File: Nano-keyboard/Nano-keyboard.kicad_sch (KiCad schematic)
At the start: 45 parts, among them J1 125SH-B-04-TS, J2 125SH-B-02-TS, U1 AMS1117, U2 ESP32-WROOM-32, U3 J5019, U4 QBC847BL, U5 EN12-HN22AF25, U6 EN12-HN22AF25, U7 QBC847BL, U8 QBC847BL

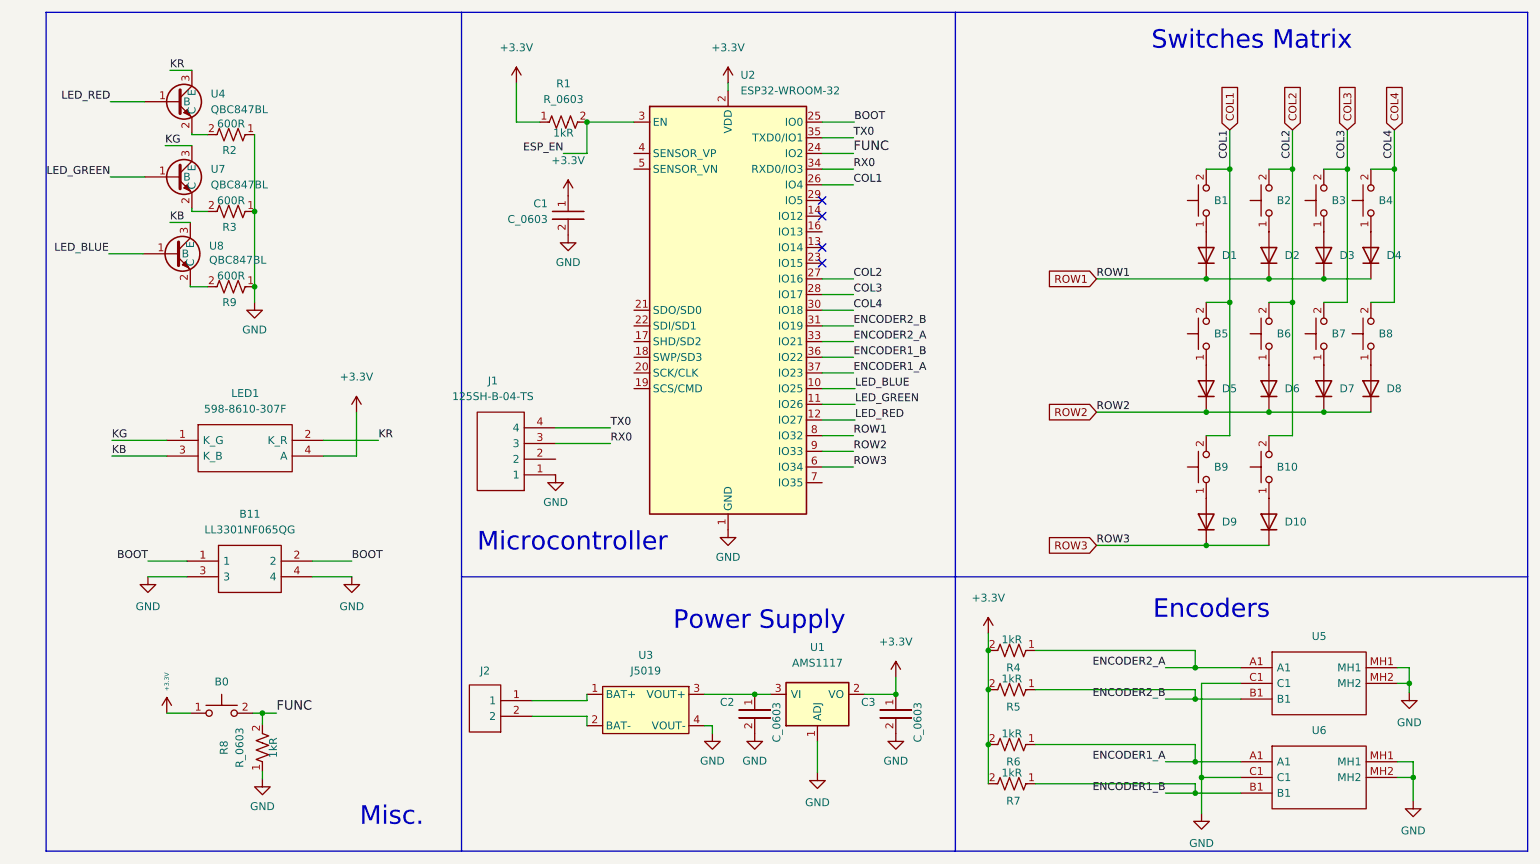
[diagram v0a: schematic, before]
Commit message: Routing of version 1.2 almest finished
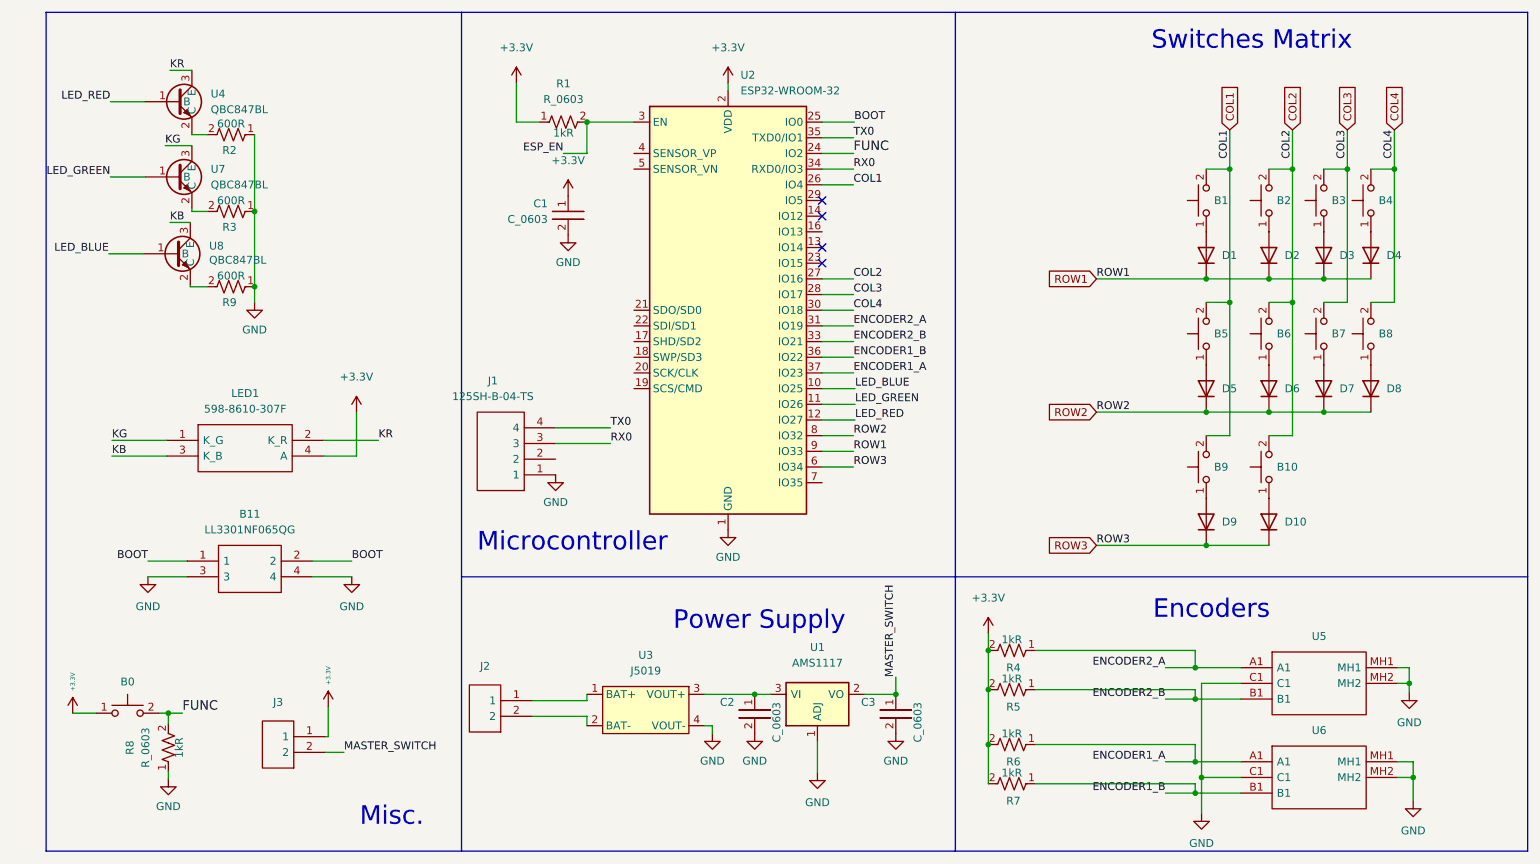
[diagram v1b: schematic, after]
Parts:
- removed J2: 125SH-B-02-TS, lib:125SHB02TS, symbol custom-keyboard:125SH-B-02-TS
- added J2, J3: 25SH-B-02-TS, lib:25SHB02TS, symbol custom-keyboard:25SH-B-02-TS
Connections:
- net +3V3: now also J3.1; no longer C3.1, U1.2 (VO)
- net ENCODER2_A: now also U2.31 (IO19); no longer U2.33 (IO21)
- net ENCODER2_B: now also U2.33 (IO21); no longer U2.31 (IO19)
- net ROW1: now also U2.9 (IO33); no longer U2.8 (IO32)
- net ROW2: now also U2.8 (IO32); no longer U2.9 (IO33)
- net at U3.1 (BAT+): now also J2.1
- net at U3.2 (BAT-): now also J2.2
- new net MASTER_SWITCH: C3.1, J3.2, U1.2 (VO)
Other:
- moved on the sheet: B0, R8

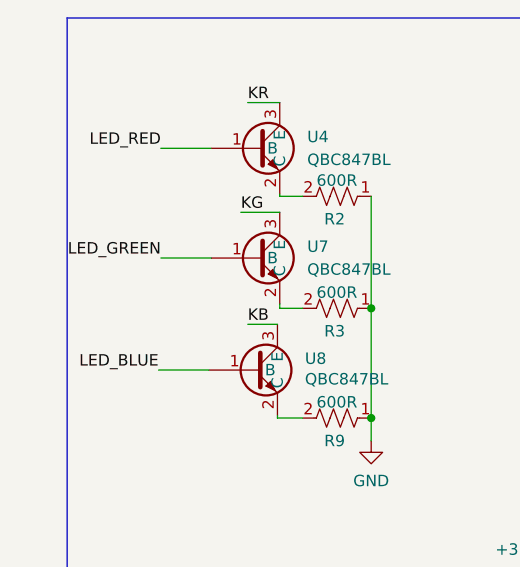
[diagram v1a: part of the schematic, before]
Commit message: Addded more spacing between keys and encoder
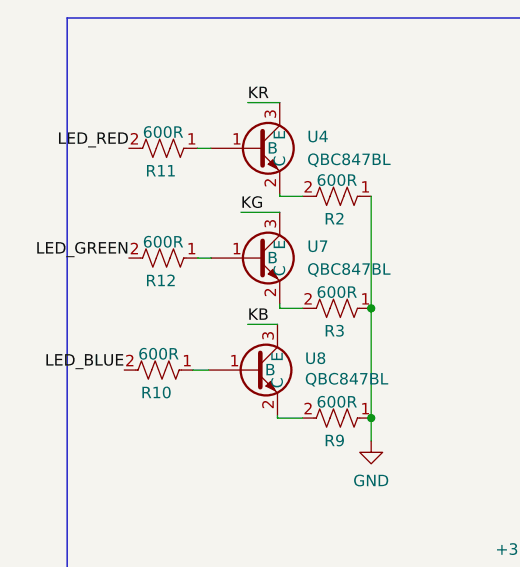
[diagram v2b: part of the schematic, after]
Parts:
- added R10, R11, R12: R_0603, lib:R_0603_1608Metric, symbol custom-keyboard:R_0603
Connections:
- net LED_BLUE: now also R10.2; no longer U8.1 (B)
- net LED_GREEN: now also R12.2; no longer U7.1 (B)
- net LED_RED: now also R11.2; no longer U4.1 (B)
- new net: R11.1, U4.1 (B)
- new net: R10.1, U8.1 (B)
- new net: R12.1, U7.1 (B)
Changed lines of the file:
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@@
     (stroke (width 0) (type default) (color 0 0 0 0))
   )
-  (wire (pts (xy 46.228 67.056) (xy 40.64 67.056))
+  (wire (pts (xy 46.228 67.056) (xy 44.45 67.056))
     (stroke (width 0) (type default) (color 0 0 0 0))
   )
@@
     (stroke (width 0) (type default) (color 0 0 0 0))
   )
-  (wire (pts (xy 46.482 54.61) (xy 40.894 54.61))
+  (wire (pts (xy 46.482 54.61) (xy 44.958 54.61))
     (stroke (width 0) (type default) (color 0 0 0 0))
   )
@@
     (stroke (width 0) (type default) (color 0 0 0 0))
   )
-  (wire (pts (xy 46.482 42.418) (xy 40.894 42.418))
+  (wire (pts (xy 46.482 42.418) (xy 44.958 42.418))
     (stroke (width 0) (type default) (color 0 0 0 0))
   )
@@
     (effects (font (size 1.27 1.27)) (justify left bottom))
   )
+  (label "LED_RED" (at 37.338 42.418 180)
+    (effects (font (size 1.27 1.27)) (justify right bottom))
+  )
   (label "MASTER_SWITCH" (at 78.74 147.828 0)
     (effects (font (size 1.27 1.27)) (justify left bottom))
@@
     (effects (font (size 1.27 1.27)) (justify left bottom))
   )
-  (label "LED_BLUE" (at 40.64 67.056 180)
-    (effects (font (size 1.27 1.27)) (justify right bottom))
-  )
   (label "ESP_EN" (at 114.3 50.8 180)
     (effects (font (size 1.27 1.27)) (justify right bottom))
@@
     (effects (font (size 1.27 1.27)) (justify left bottom))
   )
+  (label "LED_GREEN" (at 37.338 54.61 180)
+    (effects (font (size 1.27 1.27)) (justify right bottom))
+  )
   (label "FUNC" (at 52.578 141.478 0)
     (effects (font (size 1.524 1.524)) (justify left bottom))
@@
     (effects (font (size 1.27 1.27)) (justify left bottom))
   )
+  (label "LED_BLUE" (at 36.83 67.056 180)
+    (effects (font (size 1.27 1.27)) (justify right bottom))
+  )
   (label "KB" (at 41.148 99.822 0)
     (effects (font (size 1.27 1.27)) (justify left bottom))
@@
     (effects (font (size 1.27 1.27)) (justify right bottom))
   )
-  (label "LED_RED" (at 40.894 42.418 180)
-    (effects (font (size 1.27 1.27)) (justify right bottom))
-  )
   (label "BOOT" (at 46.99 116.84 180)
     (effects (font (size 1.27 1.27)) (justify right bottom))
@@
   (label "ROW3" (at 200.66 114.3 0)
     (effects (font (size 1.27 1.27)) (justify left bottom))
-  )
-  (label "LED_GREEN" (at 40.894 54.61 180)
-    (effects (font (size 1.27 1.27)) (justify right bottom))
   )
   (label "RX0" (at 121.92 97.79 0)
@@
     )
     (pin "1")
+  )
+  (symbol (lib_id "custom-keyboard:R_0603") (at 41.402 42.418 270) (unit 1)
+    (in_bom yes) (on_board yes)
+    (property "Reference" "R11" (id 0) (at 40.894 44.958 90))
+    (property "Value" "R_0603" (id 1) (at 41.148 46.101 90)
+      (effects (font (size 1.27 1.27)) hide)
+    )
+    (property "Footprint" "lib:R_0603_1608Metric" (id 2) (at 41.402 42.418 0)
+      (effects (font (size 1.27 1.27)) hide)
+    )
+    (property "Datasheet" "" (id 3) (at 41.402 42.418 0)
+      (effects (font (size 1.27 1.27)) hide)
+    )
+    (property "Resistance" "600R" (id 4) (at 41.148 41.402 90)
+      (effects (font (size 1.27 1.27)) (justify bottom))
+    )
+    (pin "1")
+    (pin "2")
   )
   (symbol (lib_id "custom-keyboard:Cherry_Switch_1U_PCB") (at 237.49 58.42 90) (unit 1)
@@
     (pin "2")
   )
+  (symbol (lib_id "custom-keyboard:R_0603") (at 40.894 67.056 270) (unit 1)
+    (in_bom yes) (on_board yes)
+    (property "Reference" "R10" (id 0) (at 40.386 69.596 90))
+    (property "Value" "R_0603" (id 1) (at 40.64 70.739 90)
+      (effects (font (size 1.27 1.27)) hide)
+    )
+    (property "Footprint" "lib:R_0603_1608Metric" (id 2) (at 40.894 67.056 0)
+      (effects (font (size 1.27 1.27)) hide)
+    )
+    (property "Datasheet" "" (id 3) (at 40.894 67.056 0)
+      (effects (font (size 1.27 1.27)) hide)
+    )
+    (property "Resistance" "600R" (id 4) (at 40.64 66.04 90)
+      (effects (font (size 1.27 1.27)) (justify bottom))
+    )
+    (pin "1")
+    (pin "2")
+  )
   (symbol (lib_id "custom-keyboard:EN12-HN22AF25") (at 224.028 134.112 0) (unit 1)
     (in_bom yes) (on_board yes) (fields_autoplaced)
@@
     (pin "2")
   )
+  (symbol (lib_id "custom-keyboard:R_0603") (at 41.402 54.61 270) (unit 1)
+    (in_bom yes) (on_board yes)
+    (property "Reference" "R12" (id 0) (at 40.894 57.15 90))
+    (property "Value" "R_0603" (id 1) (at 41.148 58.293 90)
+      (effects (font (size 1.27 1.27)) hide)
+    )
+    (property "Footprint" "lib:R_0603_1608Metric" (id 2) (at 41.402 54.61 0)
+      (effects (font (size 1.27 1.27)) hide)
+    )
+    (property "Datasheet" "" (id 3) (at 41.402 54.61 0)
+      (effects (font (size 1.27 1.27)) hide)
+    )
+    (property "Resistance" "600R" (id 4) (at 41.148 53.594 90)
+      (effects (font (size 1.27 1.27)) (justify bottom))
+    )
+    (pin "1")
+    (pin "2")
+  )
   (symbol (lib_id "Diode:1N914") (at 245.11 88.9 90) (unit 1)
     (in_bom yes) (on_board yes) (fields_autoplaced)
@@
       (reference "R9") (unit 1) (value "R_0603") (footprint "lib:R_0603_1608Metric")
     )
+    (path "/617d4152-0a73-4f18-9844-a916f966620d"
+      (reference "R10") (unit 1) (value "R_0603") (footprint "lib:R_0603_1608Metric")
+    )
+    (path "/20f64d84-077c-4efa-8060-97cad1cc2f00"
+      (reference "R11") (unit 1) (value "R_0603") (footprint "lib:R_0603_1608Metric")
+    )
+    (path "/e17bf4b0-ce68-4f6b-81d7-ab1a0f99f854"
+      (reference "R12") (unit 1) (value "R_0603") (footprint "lib:R_0603_1608Metric")
+    )
     (path "/f54960e4-2379-4f0c-bc91-5451a1cb3928"

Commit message: Minor adjustments
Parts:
- R10, R11, R12: Resistance 600R -> 1kR
- R2: Resistance 600R -> 80R
- R3: Resistance 600R -> 480R
- R9: Resistance 600R -> 220R
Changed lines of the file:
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@@
       (effects (font (size 1.27 1.27)) hide)
     )
-    (property "Resistance" "600R" (id 4) (at 41.148 41.402 90)
+    (property "Resistance" "1kR" (id 4) (at 41.148 41.402 90)
       (effects (font (size 1.27 1.27)) (justify bottom))
     )
@@
       (effects (font (size 1.27 1.27)) hide)
     )
-    (property "Resistance" "600R" (id 4) (at 60.452 46.736 90)
+    (property "Resistance" "80R" (id 4) (at 60.452 46.736 90)
       (effects (font (size 1.27 1.27)) (justify bottom))
     )
@@
       (effects (font (size 1.27 1.27)) hide)
     )
-    (property "Resistance" "600R" (id 4) (at 60.452 71.374 90)
+    (property "Resistance" "220R" (id 4) (at 60.452 71.374 90)
       (effects (font (size 1.27 1.27)) (justify bottom))
     )
@@
       (effects (font (size 1.27 1.27)) hide)
     )
-    (property "Resistance" "600R" (id 4) (at 40.64 66.04 90)
+    (property "Resistance" "1kR" (id 4) (at 40.64 66.04 90)
       (effects (font (size 1.27 1.27)) (justify bottom))
     )
@@
       (effects (font (size 1.27 1.27)) hide)
     )
-    (property "Resistance" "600R" (id 4) (at 60.452 59.182 90)
+    (property "Resistance" "480R" (id 4) (at 60.452 59.182 90)
       (effects (font (size 1.27 1.27)) (justify bottom))
     )
@@
       (effects (font (size 1.27 1.27)) hide)
     )
-    (property "Resistance" "600R" (id 4) (at 41.148 53.594 90)
-      (effects (font (size 1.27 1.27)) (justify bottom))
-    )
+    (property "Resistance" "1kR" (id 4) (at 41.148 53.594 90)
+      (effects (font (size 1.27 1.27)) (justify bottom))
+    )

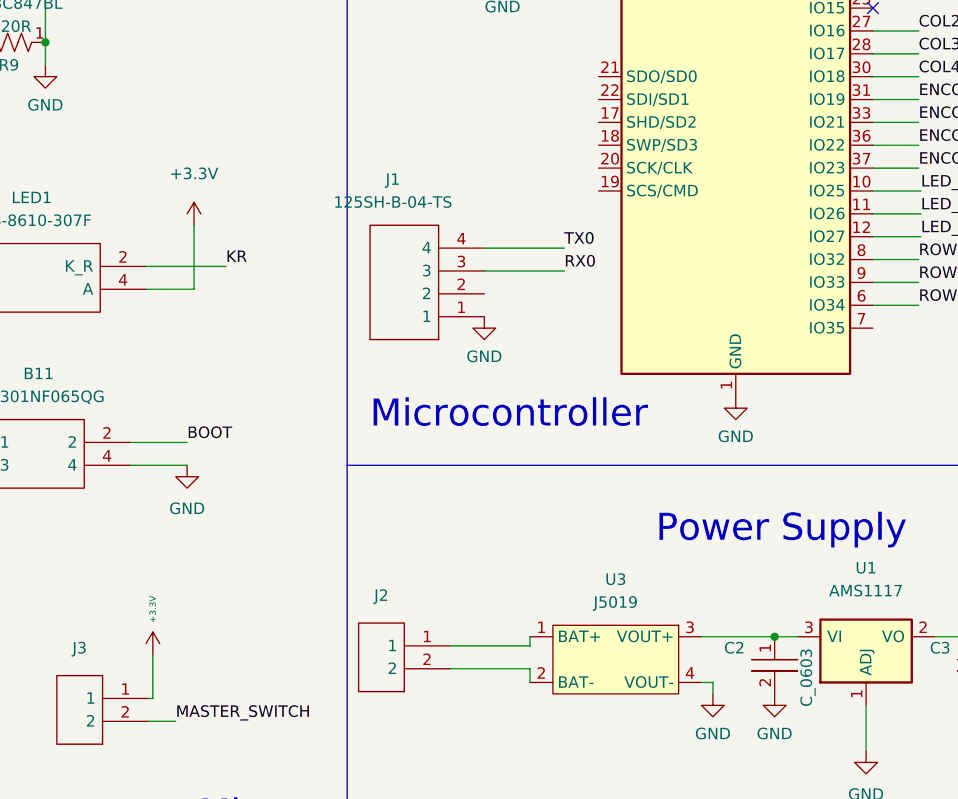
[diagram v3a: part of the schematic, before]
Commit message: [Layout] LED 5V Supply
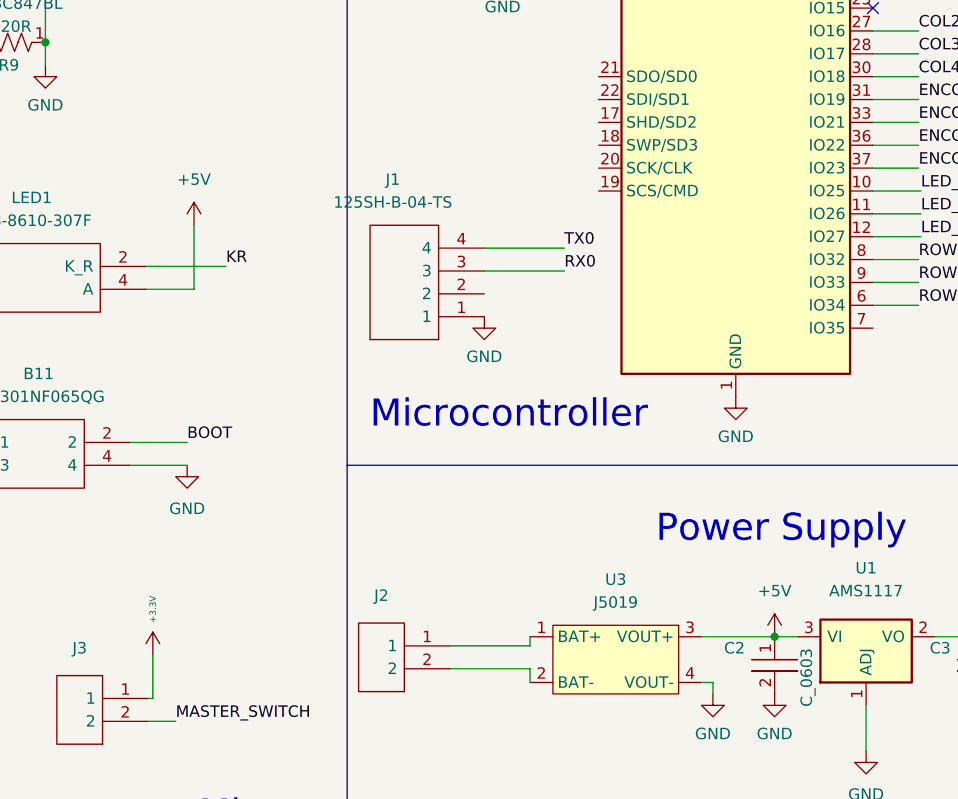
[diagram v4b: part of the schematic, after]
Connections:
- net +3V3: no longer LED1.4 (A)
- net +5V: now reaches C2.1, U1.3 (VI), U3.3 (VOUT+)
- net +5V: now also LED1.4 (A)
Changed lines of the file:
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@@
+    (stroke (width 0) (type default) (color 0 0 0 0))
+  )
+  (wire (pts (xy 137.16 138.43) (xy 145.288 138.43))
     (stroke (width 0) (type default) (color 0 0 0 0))
   )
@@
   )
   (wire (pts (xy 237.49 71.12) (xy 245.11 71.12))
-    (stroke (width 0) (type default) (color 0 0 0 0))
-  )
-  (wire (pts (xy 137.16 138.43) (xy 145.288 138.43))
     (stroke (width 0) (type default) (color 0 0 0 0))
   )
@@
     )
     (property "Datasheet" "" (id 3) (at 80.01 119.38 0)
-      (effects (font (size 1.27 1.27)) hide)
-    )
-    (pin "1")
-  )
-  (symbol (lib_id "power:+3.3V") (at 80.772 92.71 0) (unit 1)
-    (in_bom yes) (on_board yes) (fields_autoplaced)
-    (property "Reference" "#PWR015" (id 0) (at 80.772 96.52 0)
-      (effects (font (size 1.27 1.27)) hide)
-    )
-    (property "Value" "+3.3V" (id 1) (at 80.772 86.995 0))
-    (property "Footprint" "" (id 2) (at 80.772 92.71 0)
-      (effects (font (size 1.27 1.27)) hide)
-    )
-    (property "Datasheet" "" (id 3) (at 80.772 92.71 0)
       (effects (font (size 1.27 1.27)) hide)
     )
@@
     (pin "2")
   )
+  (symbol (lib_id "power:+5V") (at 80.772 92.71 0) (unit 1)
+    (in_bom yes) (on_board yes) (fields_autoplaced)
+    (property "Reference" "#PWR?" (id 0) (at 80.772 96.52 0)
+      (effects (font (size 1.27 1.27)) hide)
+    )
+    (property "Value" "+5V" (id 1) (at 80.772 87.63 0))
+    (property "Footprint" "" (id 2) (at 80.772 92.71 0)
+      (effects (font (size 1.27 1.27)) hide)
+    )
+    (property "Datasheet" "" (id 3) (at 80.772 92.71 0)
+      (effects (font (size 1.27 1.27)) hide)
+    )
+    (pin "1")
+  )
   (symbol (lib_id "power:GND") (at 155.448 151.13 0) (unit 1)
     (in_bom yes) (on_board yes) (fields_autoplaced)
@@
     )
     (property "Datasheet" "" (id 3) (at 115.062 64.008 0)
+      (effects (font (size 1.27 1.27)) hide)
+    )
+    (pin "1")
+  )
+  (symbol (lib_id "power:+5V") (at 145.288 138.43 0) (unit 1)
+    (in_bom yes) (on_board yes) (fields_autoplaced)
+    (property "Reference" "#PWR?" (id 0) (at 145.288 142.24 0)
+      (effects (font (size 1.27 1.27)) hide)
+    )
+    (property "Value" "+5V" (id 1) (at 145.288 133.35 0))
+    (property "Footprint" "" (id 2) (at 145.288 138.43 0)
+      (effects (font (size 1.27 1.27)) hide)
+    )
+    (property "Datasheet" "" (id 3) (at 145.288 138.43 0)
       (effects (font (size 1.27 1.27)) hide)
     )
@@
       (reference "#PWR014") (unit 1) (value "GND") (footprint "")
     )
-    (path "/0def1872-a33d-4b0a-8624-81ca82674c1d"
-      (reference "#PWR015") (unit 1) (value "+3.3V") (footprint "")
-    )
     (path "/e95b1d8e-2e4e-4877-9121-2ee2965866b4"
       (reference "#PWR0101") (unit 1) (value "+3.3V") (footprint "")
@@
       (reference "#PWR0107") (unit 1) (value "GND") (footprint "")
     )
+    (path "/a3dc1768-eb96-4ff6-826c-30b194ae7775"
+      (reference "#PWR?") (unit 1) (value "+5V") (footprint "")
+    )
+    (path "/bfdcb03e-e24c-48fc-8dfe-69f038f2ff51"
+      (reference "#PWR?") (unit 1) (value "+5V") (footprint "")
+    )
     (path "/e891b433-8f8c-451a-9a1f-eebc6bd34030"
